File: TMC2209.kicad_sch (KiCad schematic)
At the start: 26 parts, among them J11 Stepper, U7 TMC2209-LA

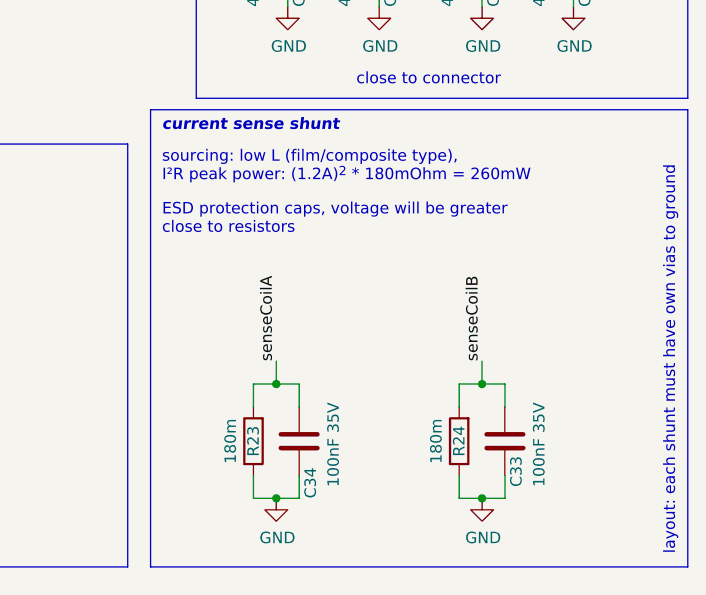
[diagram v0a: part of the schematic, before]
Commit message: Add BOM and update some values due component order
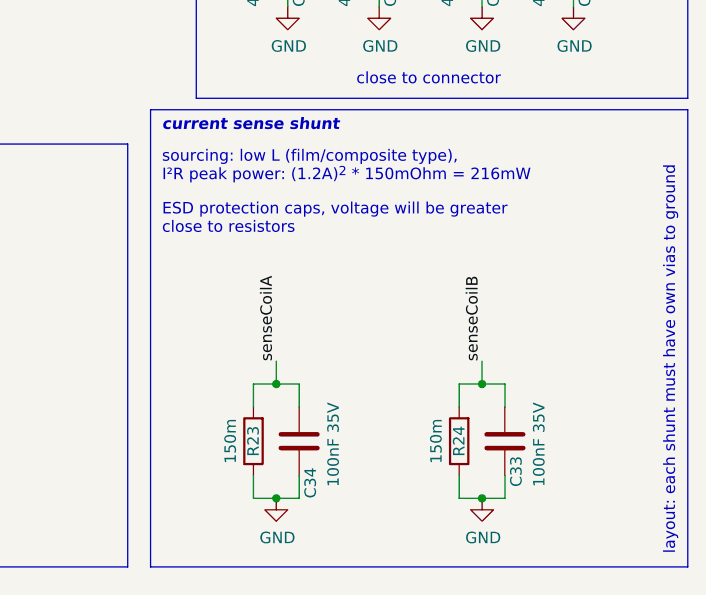
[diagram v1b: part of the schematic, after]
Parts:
- R23, R24: value 180m -> 150m
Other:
- note added: "sourcing: low L (film/composite type), I²R peak power: (1.2A)^{2} * 150mOhm = 216mW"
- note removed: "sourcing: low L (film/composite type), I²R peak power: (1.2A)^{2} * 180mOhm = 260mW"
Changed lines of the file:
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@@
     (effects (font (size 1.27 1.27)) (justify left bottom))
   )
-  (text "sourcing: low L (film/composite type), \nI²R peak power: (1.2A)^{2} * 180mOhm = 260mW \n\n"
+  (text "sourcing: low L (film/composite type), \nI²R peak power: (1.2A)^{2} * 150mOhm = 216mW \n\n"
     (at 224.79 123.19 0)
     (effects (font (size 1.27 1.27)) (justify left bottom))
@@
     (in_bom yes) (on_board yes)
     (property "Reference" "R23" (id 0) (at 234.95 149.86 90))
-    (property "Value" "180m" (id 1) (at 232.41 149.86 90))
+    (property "Value" "150m" (id 1) (at 232.41 149.86 90))
     (property "Footprint" "Resistor_SMD:R_0612_1632Metric" (id 2) (at 236.728 149.86 90)
       (effects (font (size 1.27 1.27)) hide)
@@
     (in_bom yes) (on_board yes)
     (property "Reference" "R24" (id 0) (at 257.81 149.86 90))
-    (property "Value" "180m" (id 1) (at 255.27 149.86 90))
+    (property "Value" "150m" (id 1) (at 255.27 149.86 90))
     (property "Footprint" "Resistor_SMD:R_0612_1632Metric" (id 2) (at 259.588 149.86 90)
       (effects (font (size 1.27 1.27)) hide)
